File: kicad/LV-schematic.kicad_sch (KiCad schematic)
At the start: 19 parts, among them J1 Brake motor JST, J2 Aux analog JST, J3 Steer motor JST, J4 Power JST, J5 On/off JST, J6 Throttle JST, J7 Encoder JST, J8 Steer trq & ang JST, SW1 ON/OFF, U1 Mecostrain2038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

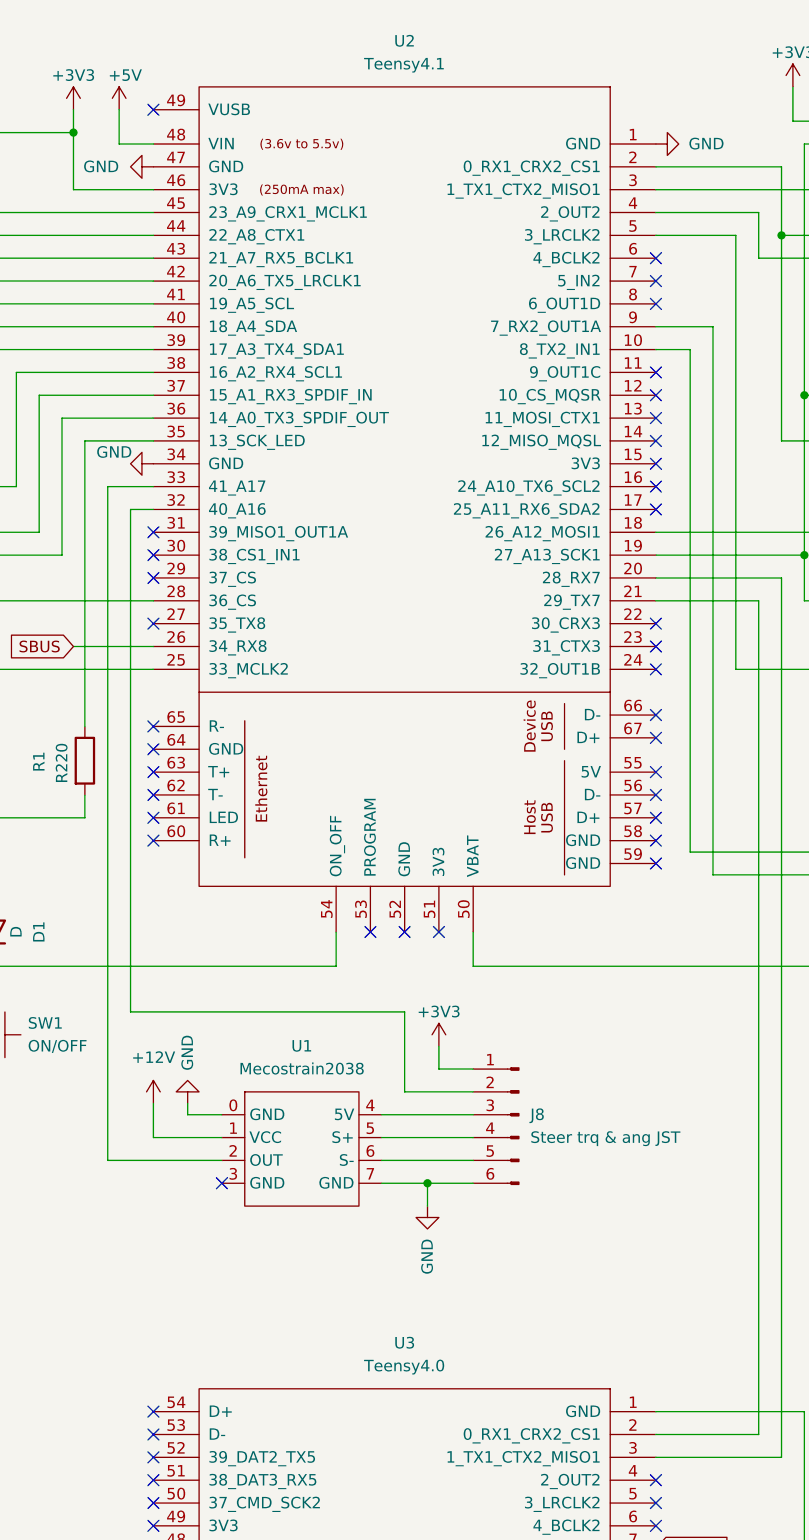
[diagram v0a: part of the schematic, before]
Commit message: Update kicad
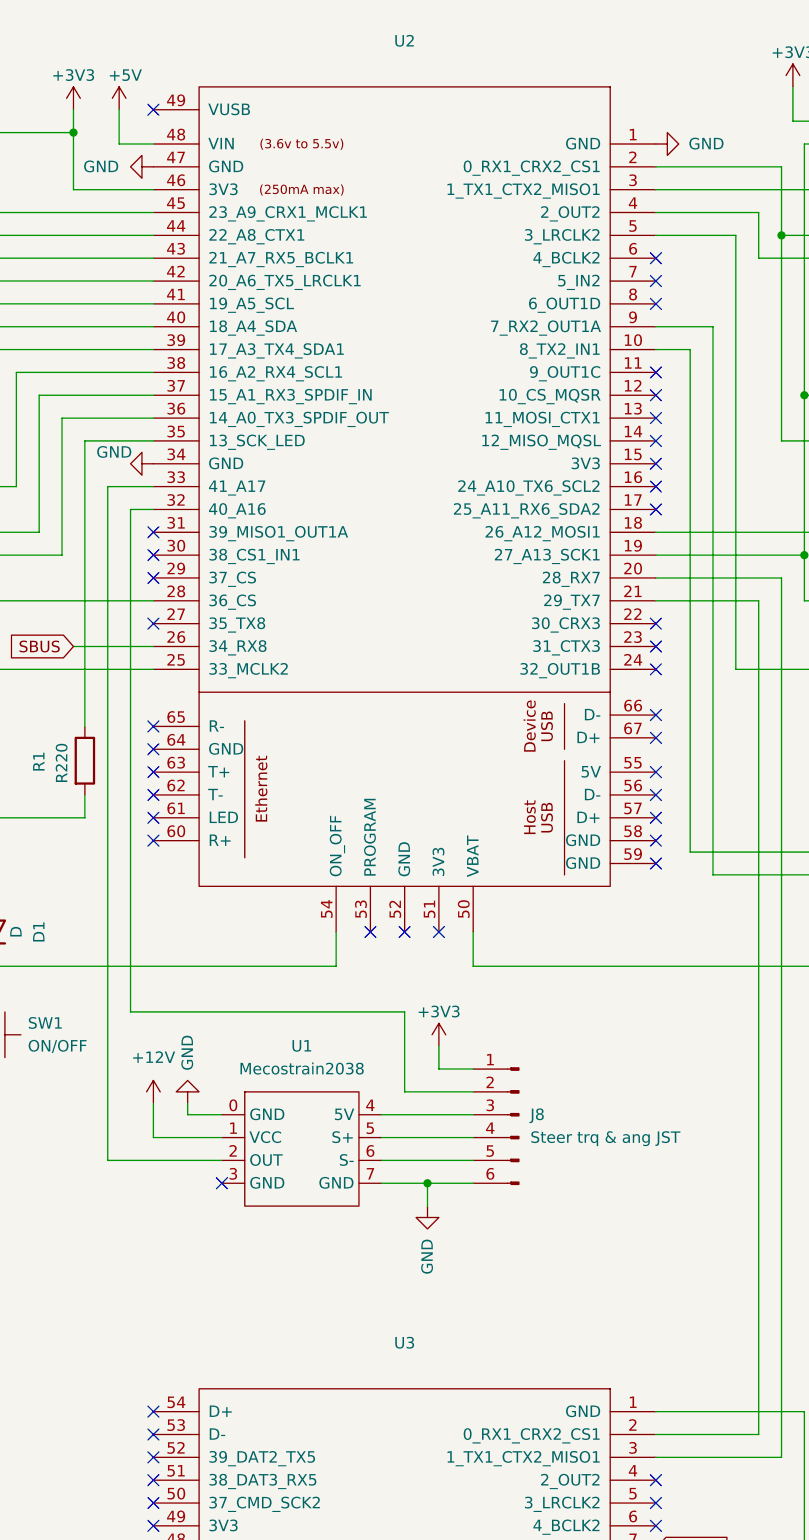
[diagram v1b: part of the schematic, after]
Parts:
- U2: value Teensy4.1 -> (none); footprint Teensy:Teensy41 -> (none)
- U3: value Teensy4.0 -> (none)
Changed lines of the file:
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@@
     (in_bom yes) (on_board yes) (fields_autoplaced)
     (property "Reference" "U3" (id 0) (at 105.41 163.83 0))
-    (property "Value" "Teensy4.0" (id 1) (at 105.41 166.37 0))
+    (property "Value" "" (id 1) (at 105.41 166.37 0))
     (property "Footprint" "" (id 2) (at 115.57 200.66 0)
       (effects (font (size 1.27 1.27)) hide)
@@
     (in_bom yes) (on_board yes) (fields_autoplaced)
     (property "Reference" "U2" (id 0) (at 105.41 19.05 0))
-    (property "Value" "Teensy4.1" (id 1) (at 105.41 21.59 0))
-    (property "Footprint" "Teensy:Teensy41" (id 2) (at 115.57 74.93 0)
-      (effects (font (size 1.27 1.27)) hide)
-    )
+    (property "Value" "" (id 1) (at 105.41 21.59 0))
+    (property "Footprint" "" (id 2) (at 115.57 74.93 0)
+      (effects (font (size 1.27 1.27)) hide)
+    )

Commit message: Update kicad and doc
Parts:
- D1: footprint (none) -> Diode_THT:D_DO-34_SOD68_P7.62mm_Horizontal
- J1: value Brake motor JST -> Brake mtr JST; footprint (none) -> Connector_JST_inches:JST_1x04_P2.54
- J2, J4, U8: footprint (none) -> Connector_JST_inches:JST_1x04_P2.54
- J3: value Steer motor JST -> Steer mtr JST; footprint (none) -> Connector_JST_inches:JST_1x06_P2.54
- J5: footprint (none) -> Connector_JST_inches:JST_1x03_P2.54
- J6: footprint (none) -> Connector_JST_inches:JST_1x02_P2.54
- J7: footprint (none) -> Connector_JST_inches:JST_1x05_P2.54
- J8: footprint (none) -> Connector_JST_inches:JST_1x06_P2.54
- R1: footprint (none) -> Resistor_THT:R_Axial_DIN0204_L3.6mm_D1.6mm_P5.08mm_Horizontal
- SW1: footprint (none) -> Button_Switch_THT:SW_PUSH_6mm
- U1: footprint (none) -> SBBMicro:Mecostrain-2038
- U2: value (none) -> Teensy4.1; footprint (none) -> teensy:Teensy41
- U3: value (none) -> Teensy4.0; footprint (none) -> teensy:Teensy40
- U4: footprint (none) -> SBBMicro:ISM330DHCX; symbol sbbmicro:ISM330DHCX -> SBBMicro:ISM330DHCX
- U5: footprint (none) -> SBBMicro:LIS3MDL
- U6: footprint (none) -> SBBMicro:MCP4922-AK
- U7: footprint (none) -> SBBMicro:Ultimate-GPS
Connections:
- net +3V3: now also U6.7 (VCC), U7.2 (VCC), U8.2 (VCC); no longer U6.1 (VCC), U7.1 (VCC), U8.1 (VCC)
- net GND: now also U1.2 (GND), U4.3 (GND), U5.3 (GND), U6.1 (GND), U6.3 (LDAC), U7.3 (GND), U8.1 (GND); no longer U1.0 (GND), U1.7 (GND), U4.0 (GND), U5.0 (GND), U6.0 (GND), U6.6 (LDAC), U7.0 (GND), U8.0 (GND)
- net SBUS: now also U8.4 (SO); no longer U8.3 (SO)
- net THR_REF: now also U6.9 (OUTB); no longer U6.11 (OUTB)
- net at U2.33 (41_A17): now also U1.3 (OUT); no longer U1.2 (OUT)
- net at U2.10 (8_TX2_IN1): now also U7.4 (RX); no longer U7.3 (RX)
- net at U2.9 (7_RX2_OUT1A): now also U7.5 (TX); no longer U7.4 (TX)
- net at U7.6 (FIX): no longer U2.50 (VBAT)
- net at U7.7 (VBAT): now also U2.50 (VBAT)
- net at U6.4 (CS): now also U2.5 (3_LRCLK2)
- net at U6.5 (MOSI): now also U2.18 (26_A12_MOSI1), U4.5 (MOSI), U5.5 (MOSI); no longer U2.5 (3_LRCLK2)
- net at U4.4 (SCK): now also U2.19 (27_A13_SCK1), U5.4 (SCK), U6.6 (SCK); no longer U2.3 (1_TX1_CTX2_MISO1)
- net at U4.6 (MISO): now also U2.3 (1_TX1_CTX2_MISO1)
- net at U4.7 (CS): now also U2.2 (0_RX1_CRX2_CS1), U5.8 (MISO)
- net at U2.4 (2_OUT2): now also U5.7 (CS); no longer U5.5 (CS)
- now unconnected: U4.2 (SCK), U5.2 (SCK), U6.2 (SCK)
- no-connect marks 91 -> 93

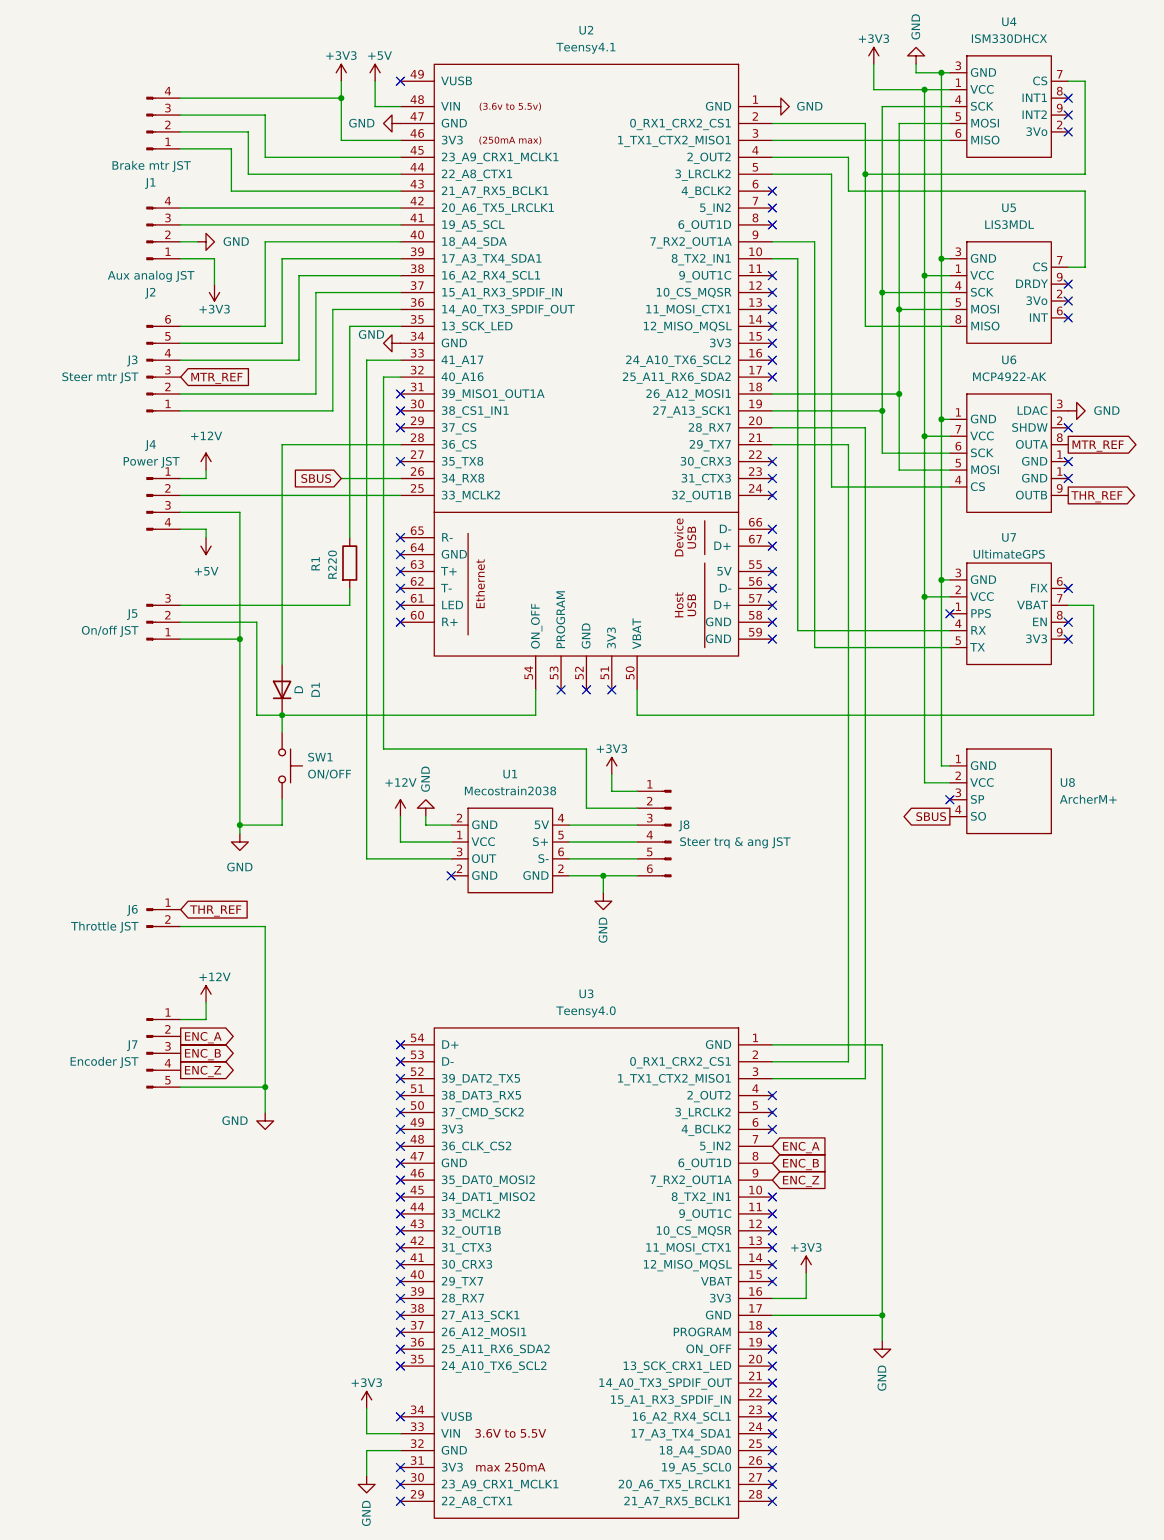
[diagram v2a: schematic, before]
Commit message: Update kicad
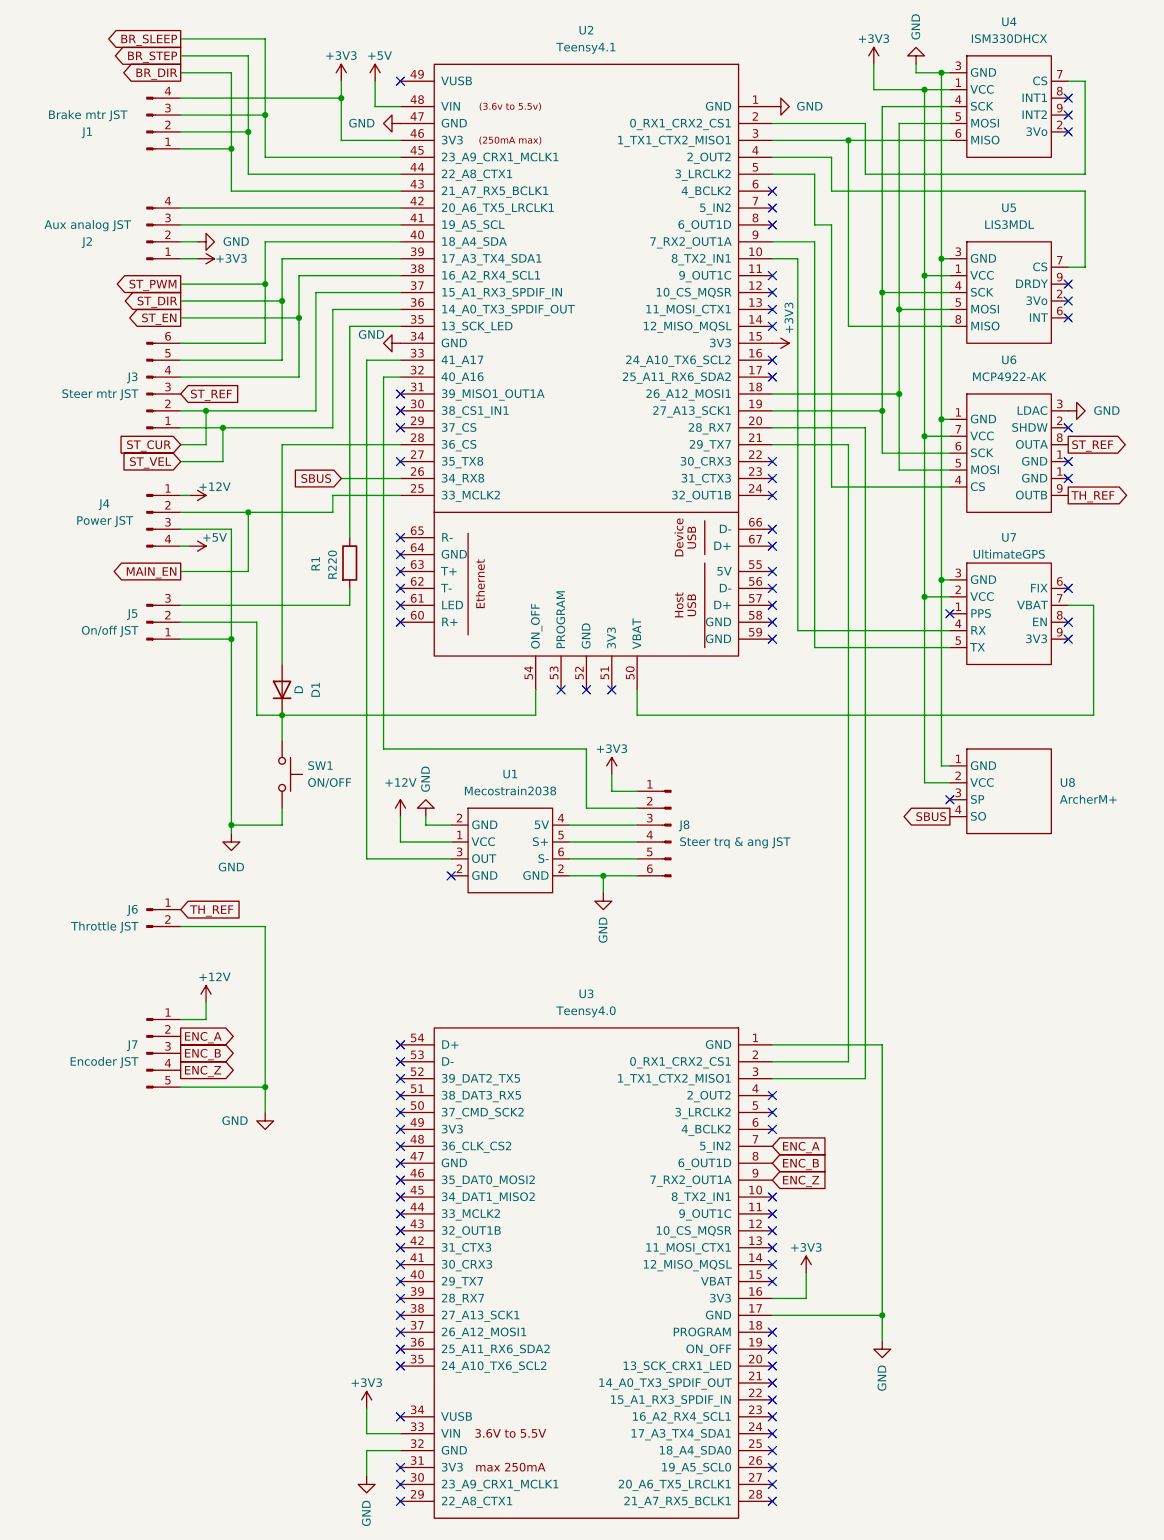
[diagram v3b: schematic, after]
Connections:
- net +3V3: now also U2.15 (3V3)
- net at U2.3 (1_TX1_CTX2_MISO1), U4.6 (MISO): now also U5.8 (MISO)
- net at U2.2 (0_RX1_CRX2_CS1), U4.7 (CS): no longer U5.8 (MISO)
- net BR_DIR: now reaches J1.1 (Pin_1), U2.43 (21_A7_RX5_BCLK1)
- net BR_STEP: now reaches J1.2 (Pin_2), U2.44 (22_A8_CTX1)
- net BR_SLEEP: now reaches J1.3 (Pin_3), U2.45 (23_A9_CRX1_MCLK1)
- net ST_VEL: now reaches J3.1 (Pin_1), U2.36 (14_A0_TX3_SPDIF_OUT)
- net ST_CUR: now reaches J3.2 (Pin_2), U2.37 (15_A1_RX3_SPDIF_IN)
- net ST_EN: now reaches J3.4 (Pin_4), U2.38 (16_A2_RX4_SCL1)
- net ST_DIR: now reaches J3.5 (Pin_5), U2.39 (17_A3_TX4_SDA1)
- net ST_PWM: now reaches J3.6 (Pin_6), U2.40 (18_A4_SDA)
- net MAIN_EN: now reaches J4.2 (Pin_2), U2.25 (33_MCLK2)
- net MTR_REF renamed ST_REF
- net THR_REF renamed TH_REF
- no-connect marks 93 -> 92
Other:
- moved on the sheet: J3, J4, SW1
